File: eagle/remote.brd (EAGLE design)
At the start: 75.9 x 72.4 mm, 22 parts, among them IC1 7805TV, Q1 16 Mhz, U1 ATMEGA328P-PU

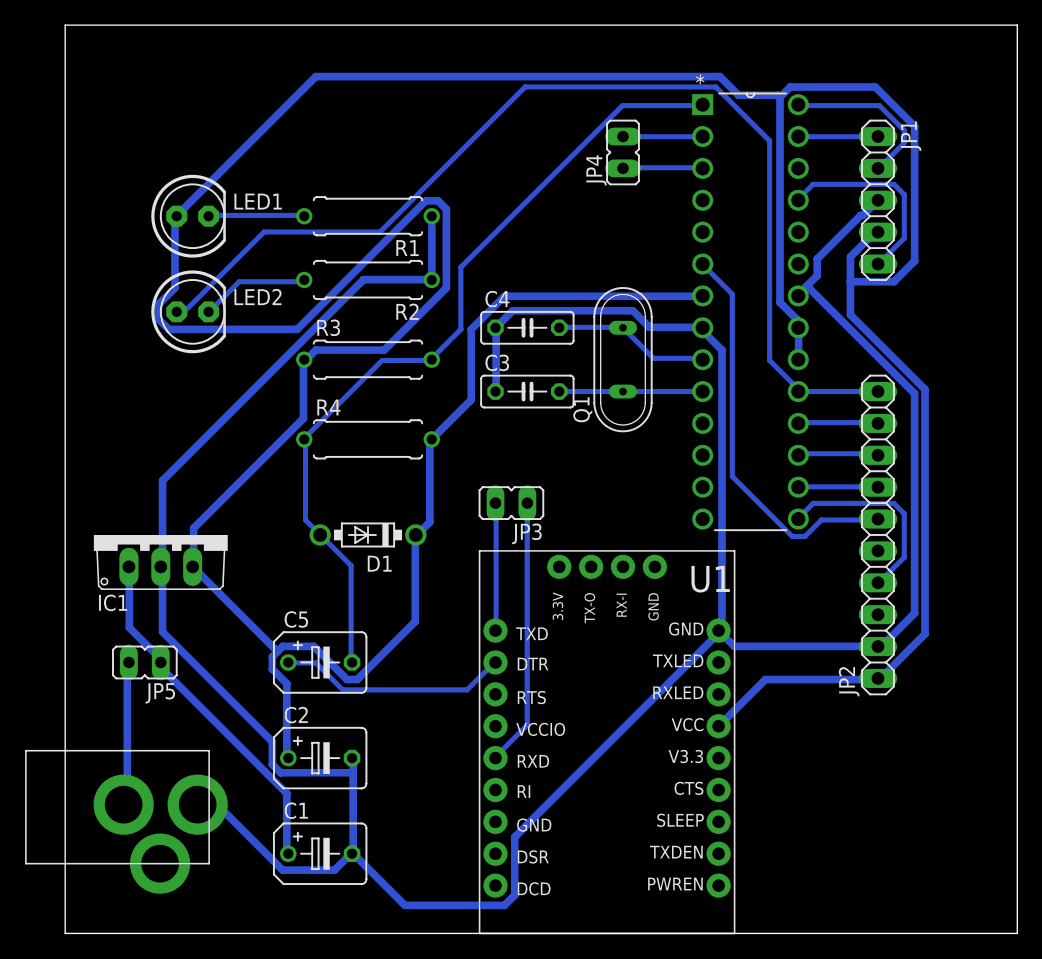
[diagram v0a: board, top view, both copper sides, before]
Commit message: Reworked PCB so it is smaller.
Because I plan to order the PCB using www.oshpark.com, I used two layers
and tightened everything up.
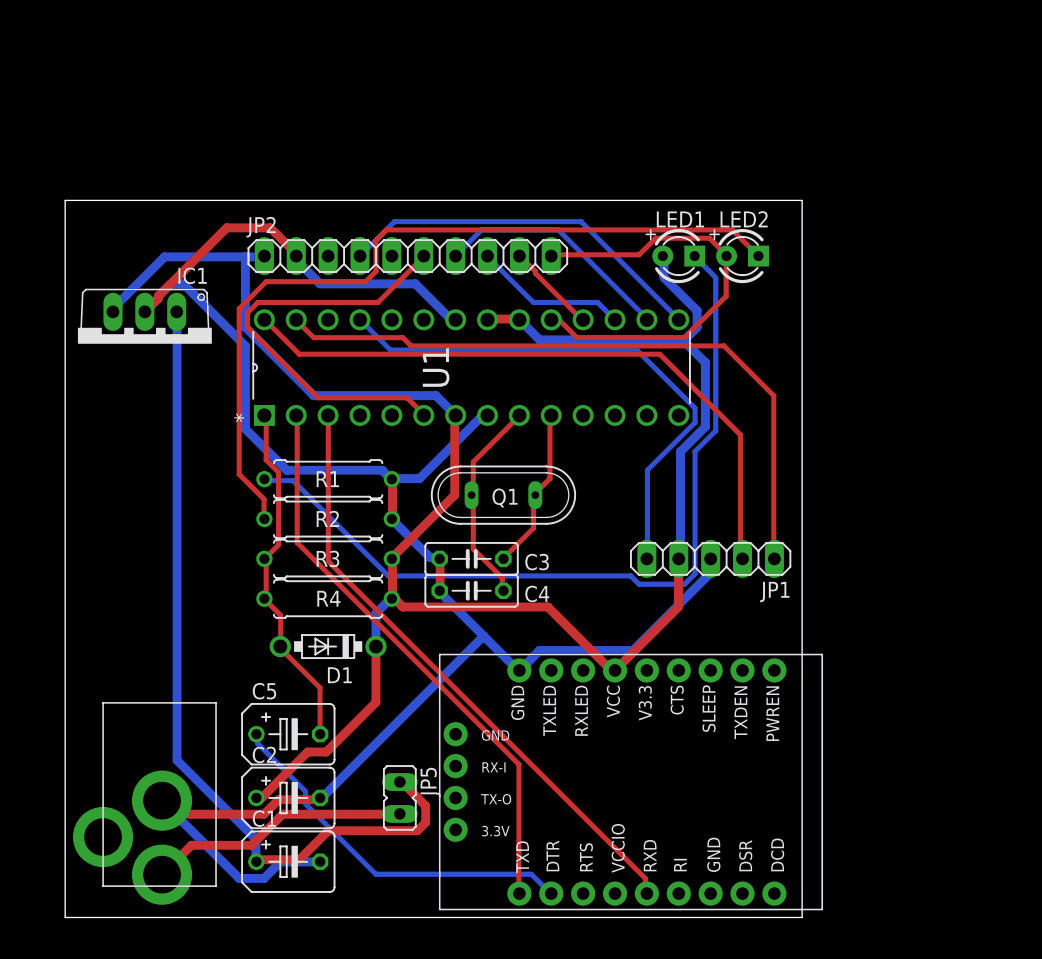
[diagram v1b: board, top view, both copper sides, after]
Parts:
- removed JP3, JP4: (no value), jumper:JP1
- LED1, LED2: device adafruit:LED5MM -> EE445L:LED3MM
- R1, R2: value 220 -> 330
- moved LED2 44.0 mm to (54.0, 60.3)
- moved JP2 43.6 mm to (27.3, 60.3), turned to 0 degrees
- moved LED1 38.9 mm to (48.9, 60.3)
- moved JP1 31.5 mm to (51.4, 36.2), turned to 180 degrees
- moved JP5 23.0 mm to (26.7, 17.1), turned to 180 degrees
- moved C4 21.4 mm to (32.4, 33.7)
- moved R1 21.2 mm to (21.0, 42.5)
- moved R2 19.3 mm to (21.0, 39.4)
- moved U1 18.5 mm to (48.9, 55.2), turned to 90 degrees
- moved R3 16.2 mm to (21.0, 36.2), turned to 180 degrees
- moved IC1 15.3 mm to (6.35, 53.3), turned to 180 degrees
- moved Q1 14.4 mm to (34.9, 41.3), turned to 180 degrees
- moved C3 14.1 mm to (32.4, 36.2)
- moved R4 13.1 mm to (21.0, 33.0)
- moved D1 9.44 mm to (21.0, 29.2)
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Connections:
- removed net N$3: JP3.1, U$1.RXD
- removed net N$6: JP3.2, U$1.TXD
- net GND: now also 9V-JACK.RING; no longer 9V-JACK.TIP
- net N$8: now also 9V-JACK.TIP; no longer 9V-JACK.RING
- net RXD: now also U$1.RXD; no longer JP4.1
- net TXD: now also U$1.TXD; no longer JP4.2
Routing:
- net 5V: track 313.1 -> 152.4 mm
- net GND: track 236.7 -> 159.0 mm
- net N$2: track 7.66 -> 64.8 mm
- net N$9: track 8.70 -> 63.9 mm
- net SCK: track 83.8 -> 34.3 mm
- net SDA: track 6.35 -> 53.6 mm
- net RXD: track 6.37 -> 48.7 mm
- net TXD: track 6.35 -> 45.5 mm
- net SCL: track 13.2 -> 51.7 mm
- net N$1: track 28.2 -> 65.5 mm
- net RESET: track 65.1 -> 28.4 mm
- net INT: track 15.8 -> 43.2 mm
- net N$3: track 21.4 -> 0.00 mm
- net RST: track 15.7 -> 29.8 mm
- net REQ: track 6.37 -> 19.2 mm
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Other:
- board size 75.9 x 72.4 mm -> 58.7 x 57.1 mm
